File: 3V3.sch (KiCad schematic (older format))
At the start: 5 parts

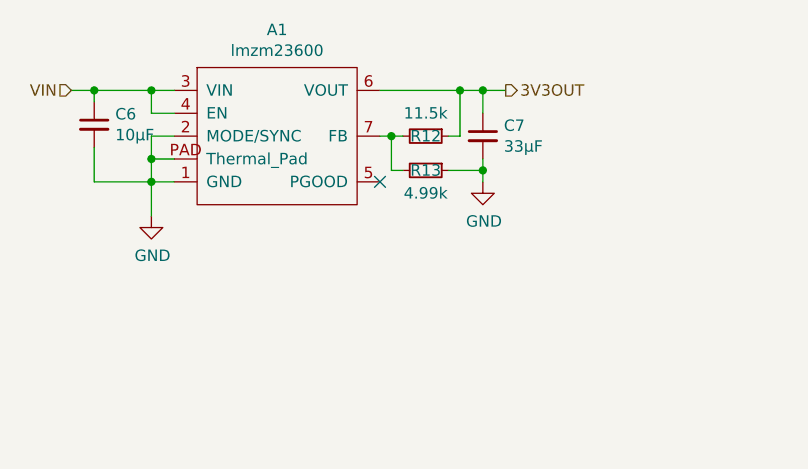
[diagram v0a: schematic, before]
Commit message: LMZM23600 from official kicad lib
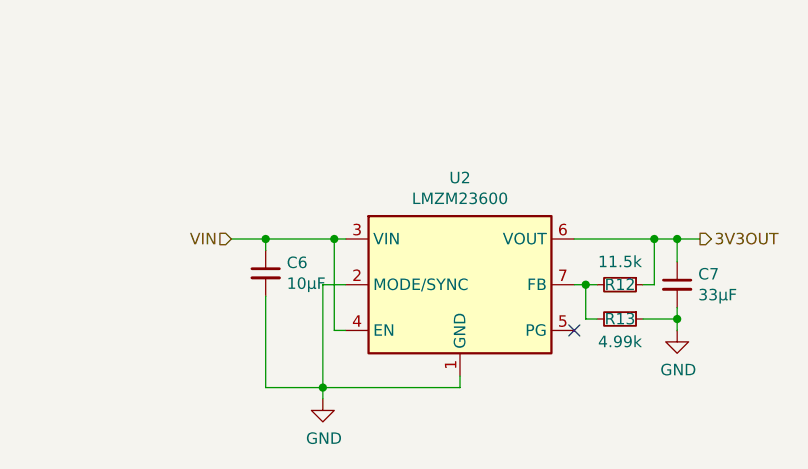
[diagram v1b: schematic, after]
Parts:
- removed A1: lmzm23600, LMZM23600:lmzm23600, symbol lmzm23600:lmzm23600
- added U2: LMZM23600, Package_LGA:Texas_SIL0010A_MicroSiP-10-1EP_3.8x3mm_P0.6mm_EP0.7x2.9mm_ThermalVias, symbol Regulator_Switching:LMZM23600
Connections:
- net 3V3OUT: now also U2.6 (VOUT)
- net GND: now also U2.1 (GND), U2.11 (GND), U2.2 (MODE/SYNC)
- net VIN: now also U2.3 (VIN), U2.4 (EN)
- net at R12.2, R13.2: now also U2.7 (FB)
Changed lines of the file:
@@
 $EndDescr
 $Comp
-L lmzm23600:lmzm23600 A?
-U 1 1 5C2CE8BB
-P 4350 2150
-AR Path="/5C2CE8BB" Ref="A?"  Part="1"
-AR Path="/5C2CDDAC/5C2CE8BB" Ref="A?"  Part="1"
-AR Path="/5C920C0A/5C2CE8BB" Ref="A1"  Part="1"
-F 0 "A1" H 4350 2615 50  0000 C CNN
-F 1 "lmzm23600" H 4350 2524 50  0000 C CNN
-F 2 "LMZM23600:lmzm23600" H 4350 2150 50  0001 C CNN
-F 3 "" H 4350 2150 50  0001 C CNN
-	1    4350 2150
-	1    0    0    -1
-$EndComp
-Wire Wire Line
-	3800 2250 3800 2350
-Wire Wire Line
-	3800 2350 3900 2350
-$Comp
-L power:GND #PWR?
-U 1 1 5C2CE8C4
-P 3800 2500
-AR Path="/5C2CE8C4" Ref="#PWR?"  Part="1"
-AR Path="/5C2CDDAC/5C2CE8C4" Ref="#PWR?"  Part="1"
-AR Path="/5C920C0A/5C2CE8C4" Ref="#PWR034"  Part="1"
-F 0 "#PWR034" H 3800 2250 50  0001 C CNN
-F 1 "GND" H 3805 2327 50  0000 C CNN
-F 2 "" H 3800 2500 50  0001 C CNN
-F 3 "" H 3800 2500 50  0001 C CNN
-	1    3800 2500
-	1    0    0    -1
-$EndComp
-Wire Wire Line
-	3800 2500 3800 2350
-Connection ~ 3800 2350
-$Comp
-L Device:C_Small C?
-U 1 1 5C2CE8DC
-P 3550 2100
-AR Path="/5C2CE8DC" Ref="C?"  Part="1"
-AR Path="/5C2CDDAC/5C2CE8DC" Ref="C?"  Part="1"
-AR Path="/5C920C0A/5C2CE8DC" Ref="C6"  Part="1"
-F 0 "C6" H 3642 2146 50  0000 L CNN
-F 1 "10µF" H 3642 2055 50  0000 L CNN
-F 2 "Capacitor_SMD:C_1210_3225Metric" H 3550 2100 50  0001 C CNN
-F 3 "~" H 3550 2100 50  0001 C CNN
-F 4 "50V" H 3550 2100 50  0001 C CNN "Voltage Rating"
-	1    3550 2100
-	1    0    0    -1
-$EndComp
-Wire Wire Line
-	3550 2200 3550 2350
-Wire Wire Line
-	3550 2350 3800 2350
-Wire Wire Line
-	3800 2150 3800 2250
-Connection ~ 3800 2250
-Wire Wire Line
-	3800 2150 3900 2150
-Wire Wire Line
-	3800 2250 3900 2250
-Wire Wire Line
-	3550 2000 3550 1950
-Wire Wire Line
-	3550 1950 3800 1950
-Connection ~ 3800 1950
-Wire Wire Line
-	3800 1950 3900 1950
-Wire Wire Line
-	3800 2050 3800 1950
-Wire Wire Line
-	3800 2050 3900 2050
-$Comp
-L Device:C_Small C?
-U 1 1 5C2CE8F0
-P 5250 2150
-AR Path="/5C2CE8F0" Ref="C?"  Part="1"
-AR Path="/5C2CDDAC/5C2CE8F0" Ref="C?"  Part="1"
-AR Path="/5C920C0A/5C2CE8F0" Ref="C7"  Part="1"
-F 0 "C7" H 5342 2196 50  0000 L CNN
-F 1 "33µF" H 5342 2105 50  0000 L CNN
-F 2 "Capacitor_SMD:C_1210_3225Metric" H 5250 2150 50  0001 C CNN
-F 3 "~" H 5250 2150 50  0001 C CNN
-F 4 "Low ESR" H 5250 2150 50  0001 C CNN "Notes"
-	1    5250 2150
+L Regulator_Switching:LMZM23600 U2
+U 1 1 5CA58FF1
+P 5150 2800
+F 0 "U2" H 5150 3267 50  0000 C CNN
+F 1 "LMZM23600" H 5150 3176 50  0000 C CNN
+F 2 "Package_LGA:Texas_SIL0010A_MicroSiP-10-1EP_3.8x3mm_P0.6mm_EP0.7x2.9mm_ThermalVias" H 5150 1950 50  0001 C CNN
+F 3 "http://www.ti.com/lit/ds/symlink/lmzm23600.pdf" H 5150 2050 50  0001 C CNN
+	1    5150 2800
 	1    0    0    -1
 $EndComp
 $Comp
 L power:GND #PWR?
-U 1 1 5C2CE8F8
-P 5250 2350
-AR Path="/5C2CE8F8" Ref="#PWR?"  Part="1"
-AR Path="/5C2CDDAC/5C2CE8F8" Ref="#PWR?"  Part="1"
-AR Path="/5C920C0A/5C2CE8F8" Ref="#PWR035"  Part="1"
-F 0 "#PWR035" H 5250 2100 50  0001 C CNN
-F 1 "GND" H 5255 2177 50  0000 C CNN
-F 2 "" H 5250 2350 50  0001 C CNN
-F 3 "" H 5250 2350 50  0001 C CNN
-	1    5250 2350
+U 1 1 5CA5C1D2
+P 4550 3300
+AR Path="/5CA5C1D2" Ref="#PWR?"  Part="1"
+AR Path="/5C2CDDAC/5CA5C1D2" Ref="#PWR?"  Part="1"
+AR Path="/5C920C0A/5CA5C1D2" Ref="#PWR034"  Part="1"
+F 0 "#PWR034" H 4550 3050 50  0001 C CNN
+F 1 "GND" H 4555 3127 50  0000 C CNN
+F 2 "" H 4550 3300 50  0001 C CNN
+F 3 "" H 4550 3300 50  0001 C CNN
+	1    4550 3300
+	1    0    0    -1
+$EndComp
+$Comp
+L Device:C_Small C?
+U 1 1 5CA5C1DF
+P 4300 2750
+AR Path="/5CA5C1DF" Ref="C?"  Part="1"
+AR Path="/5C2CDDAC/5CA5C1DF" Ref="C?"  Part="1"
+AR Path="/5C920C0A/5CA5C1DF" Ref="C6"  Part="1"
+F 0 "C6" H 4392 2796 50  0000 L CNN
+F 1 "10µF" H 4392 2705 50  0000 L CNN
+F 2 "Capacitor_SMD:C_1210_3225Metric" H 4300 2750 50  0001 C CNN
+F 3 "~" H 4300 2750 50  0001 C CNN
+F 4 "50V" H 4300 2750 50  0001 C CNN "Voltage Rating"
+	1    4300 2750
+	1    0    0    -1
+$EndComp
+$Comp
+L Device:C_Small C?
+U 1 1 5CA5C1F6
+P 6100 2800
+AR Path="/5CA5C1F6" Ref="C?"  Part="1"
+AR Path="/5C2CDDAC/5CA5C1F6" Ref="C?"  Part="1"
+AR Path="/5C920C0A/5CA5C1F6" Ref="C7"  Part="1"
+F 0 "C7" H 6192 2846 50  0000 L CNN
+F 1 "33µF" H 6192 2755 50  0000 L CNN
+F 2 "Capacitor_SMD:C_1210_3225Metric" H 6100 2800 50  0001 C CNN
+F 3 "~" H 6100 2800 50  0001 C CNN
+F 4 "Low ESR" H 6100 2800 50  0001 C CNN "Notes"
+	1    6100 2800
+	1    0    0    -1
+$EndComp
+$Comp
+L power:GND #PWR?
+U 1 1 5CA5C200
+P 6100 3000
+AR Path="/5CA5C200" Ref="#PWR?"  Part="1"
+AR Path="/5C2CDDAC/5CA5C200" Ref="#PWR?"  Part="1"
+AR Path="/5C920C0A/5CA5C200" Ref="#PWR035"  Part="1"
+F 0 "#PWR035" H 6100 2750 50  0001 C CNN
+F 1 "GND" H 6105 2827 50  0000 C CNN
+F 2 "" H 6100 3000 50  0001 C CNN
+F 3 "" H 6100 3000 50  0001 C CNN
+	1    6100 3000
 	1    0    0    -1
 $EndComp
 Wire Wire Line
-	5250 2050 5250 1950
+	6100 2700 6100 2600
 Wire Wire Line
-	5250 2250 5250 2300
+	6100 2900 6100 2950
 $Comp
 L Device:R_Small R?
-U 1 1 5C2CE900
-P 5000 2150
-AR Path="/5C2CE900" Ref="R?"  Part="1"
-AR Path="/5C2CDDAC/5C2CE900" Ref="R?"  Part="1"
-AR Path="/5C920C0A/5C2CE900" Ref="R12"  Part="1"
-F 0 "R12" V 5000 2150 50  0000 C CNN
-F 1 "11.5k" V 4900 2150 50  0000 C CNN
-F 2 "Resistor_SMD:R_0603_1608Metric" H 5000 2150 50  0001 C CNN
-F 3 "~" H 5000 2150 50  0001 C CNN
-	1    5000 2150
+U 1 1 5CA5C20C
+P 5850 2800
+AR Path="/5CA5C20C" Ref="R?"  Part="1"
+AR Path="/5C2CDDAC/5CA5C20C" Ref="R?"  Part="1"
+AR Path="/5C920C0A/5CA5C20C" Ref="R12"  Part="1"
+F 0 "R12" V 5850 2800 50  0000 C CNN
+F 1 "11.5k" V 5750 2800 50  0000 C CNN
+F 2 "Resistor_SMD:R_0603_1608Metric" H 5850 2800 50  0001 C CNN
+F 3 "~" H 5850 2800 50  0001 C CNN
+	1    5850 2800
 	0    1    1    0
 $EndComp
 Wire Wire Line
-	4800 2150 4850 2150
+	5650 2800 5700 2800
 $Comp
 L Device:R_Small R?
-U 1 1 5C2CE909
-P 5000 2300
-AR Path="/5C2CE909" Ref="R?"  Part="1"
-AR Path="/5C2CDDAC/5C2CE909" Ref="R?"  Part="1"
-AR Path="/5C920C0A/5C2CE909" Ref="R13"  Part="1"
-F 0 "R13" V 5000 2300 50  0000 C CNN
-F 1 "4.99k" V 5100 2300 50  0000 C CNN
-F 2 "Resistor_SMD:R_0603_1608Metric" H 5000 2300 50  0001 C CNN
-F 3 "~" H 5000 2300 50  0001 C CNN
-	1    5000 2300
+U 1 1 5CA5C217
+P 5850 2950
+AR Path="/5CA5C217" Ref="R?"  Part="1"
+AR Path="/5C2CDDAC/5CA5C217" Ref="R?"  Part="1"
+AR Path="/5C920C0A/5CA5C217" Ref="R13"  Part="1"
+F 0 "R13" V 5850 2950 50  0000 C CNN
+F 1 "4.99k" V 5950 2950 50  0000 C CNN
+F 2 "Resistor_SMD:R_0603_1608Metric" H 5850 2950 50  0001 C CNN
+F 3 "~" H 5850 2950 50  0001 C CNN
+	1    5850 2950
 	0    1    1    0
 $EndComp
 Wire Wire Line
-	4900 2300 4850 2300
+	5750 2950 5700 2950
 Wire Wire Line
-	4850 2300 4850 2150
-Connection ~ 4850 2150
+	5700 2950 5700 2800
+Connection ~ 5700 2800
 Wire Wire Line
-	4850 2150 4900 2150
+	5700 2800 5750 2800
 Wire Wire Line
-	5100 2300 5250 2300
-Connection ~ 5250 2300
+	5950 2950 6100 2950
+Connection ~ 6100 2950
 Wire Wire Line
-	5250 2300 5250 2350
+	6100 2950 6100 3000
 Wire Wire Line
-	5100 2150 5150 2150
+	5950 2800 6000 2800
 Wire Wire Line
-	5150 2150 5150 1950
-Connection ~ 5150 1950
+	6000 2800 6000 2600
+Connection ~ 6000 2600
 Wire Wire Line
-	5150 1950 5250 1950
-NoConn ~ 4800 2350
-Text HLabel 3450 1950 0    50   Input ~ 0
+	6000 2600 6100 2600
+NoConn ~ 5650 3000
+Text HLabel 4150 2600 0    50   Input ~ 0
 VIN
-Wire Wire Line
-	3450 1950 3550 1950
-Connection ~ 3550 1950
-Text HLabel 5350 1950 2    50   Output ~ 0
+Text HLabel 6200 2600 2    50   Output ~ 0
 3V3OUT
 Wire Wire Line
-	4800 1950 5150 1950
+	5650 2600 6000 2600
 Wire Wire Line
-	5250 1950 5350 1950
-Connection ~ 5250 1950
+	6100 2600 6200 2600
+Connection ~ 6100 2600
+Wire Wire Line
+	4650 2600 4600 2600
+Wire Wire Line
+	4300 2650 4300 2600
+Connection ~ 4300 2600
+Wire Wire Line
+	4300 2600 4150 2600
+Wire Wire Line
+	4650 3000 4600 3000
+Wire Wire Line
+	4600 3000 4600 2600
+Connection ~ 4600 2600
+Wire Wire Line
+	4600 2600 4300 2600
+Wire Wire Line
+	4650 2800 4550 2800
+Wire Wire Line
+	4550 2800 4550 3250
+Wire Wire Line
+	4550 3250 5150 3250
+Wire Wire Line
+	5150 3250 5150 3200
+Wire Wire Line
+	4300 3250 4550 3250
+Wire Wire Line
+	4300 2850 4300 3250
+Connection ~ 4550 3250
+Wire Wire Line
+	4550 3300 4550 3250
 $EndSCHEMATC

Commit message: use submodule for FT230
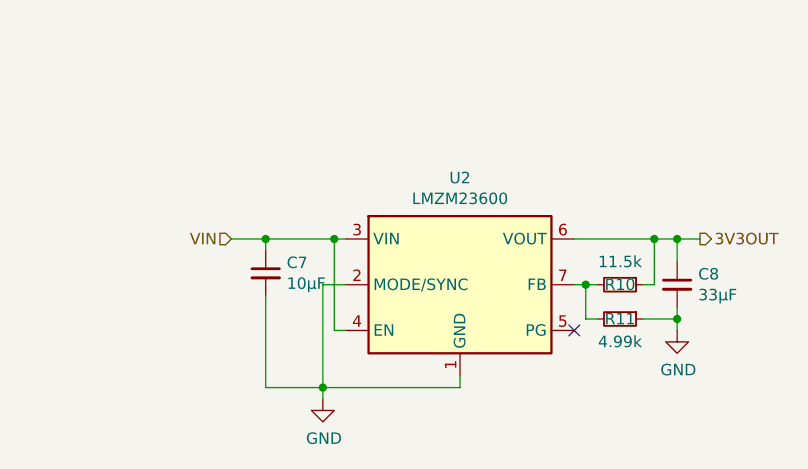
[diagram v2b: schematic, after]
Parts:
- renumbered C6 to C7, C7 to C8, R12 to R10, R13 to R11
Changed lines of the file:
@@
 AR Path="/5CA5C1DF" Ref="C?"  Part="1"
 AR Path="/5C2CDDAC/5CA5C1DF" Ref="C?"  Part="1"
-AR Path="/5C920C0A/5CA5C1DF" Ref="C6"  Part="1"
-F 0 "C6" H 4392 2796 50  0000 L CNN
+AR Path="/5C920C0A/5CA5C1DF" Ref="C7"  Part="1"
+F 0 "C7" H 4392 2796 50  0000 L CNN
 F 1 "10µF" H 4392 2705 50  0000 L CNN
 F 2 "Capacitor_SMD:C_1210_3225Metric" H 4300 2750 50  0001 C CNN
@@
 AR Path="/5CA5C1F6" Ref="C?"  Part="1"
 AR Path="/5C2CDDAC/5CA5C1F6" Ref="C?"  Part="1"
-AR Path="/5C920C0A/5CA5C1F6" Ref="C7"  Part="1"
-F 0 "C7" H 6192 2846 50  0000 L CNN
+AR Path="/5C920C0A/5CA5C1F6" Ref="C8"  Part="1"
+F 0 "C8" H 6192 2846 50  0000 L CNN
 F 1 "33µF" H 6192 2755 50  0000 L CNN
 F 2 "Capacitor_SMD:C_1210_3225Metric" H 6100 2800 50  0001 C CNN
@@
 AR Path="/5CA5C20C" Ref="R?"  Part="1"
 AR Path="/5C2CDDAC/5CA5C20C" Ref="R?"  Part="1"
-AR Path="/5C920C0A/5CA5C20C" Ref="R12"  Part="1"
-F 0 "R12" V 5850 2800 50  0000 C CNN
+AR Path="/5C920C0A/5CA5C20C" Ref="R10"  Part="1"
+F 0 "R10" V 5850 2800 50  0000 C CNN
 F 1 "11.5k" V 5750 2800 50  0000 C CNN
 F 2 "Resistor_SMD:R_0603_1608Metric" H 5850 2800 50  0001 C CNN
@@
 AR Path="/5CA5C217" Ref="R?"  Part="1"
 AR Path="/5C2CDDAC/5CA5C217" Ref="R?"  Part="1"
-AR Path="/5C920C0A/5CA5C217" Ref="R13"  Part="1"
-F 0 "R13" V 5850 2950 50  0000 C CNN
+AR Path="/5C920C0A/5CA5C217" Ref="R11"  Part="1"
+F 0 "R11" V 5850 2950 50  0000 C CNN
 F 1 "4.99k" V 5950 2950 50  0000 C CNN
 F 2 "Resistor_SMD:R_0603_1608Metric" H 5850 2950 50  0001 C CNN

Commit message: pullups, jumpers
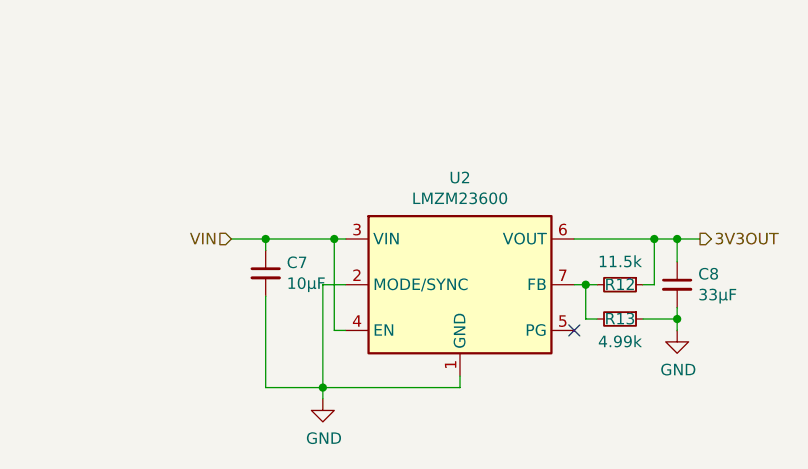
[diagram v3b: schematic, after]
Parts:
- renumbered R10 to R12, R11 to R13
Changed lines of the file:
@@
 AR Path="/5CA5C20C" Ref="R?"  Part="1"
 AR Path="/5C2CDDAC/5CA5C20C" Ref="R?"  Part="1"
-AR Path="/5C920C0A/5CA5C20C" Ref="R10"  Part="1"
-F 0 "R10" V 5850 2800 50  0000 C CNN
+AR Path="/5C920C0A/5CA5C20C" Ref="R12"  Part="1"
+F 0 "R12" V 5850 2800 50  0000 C CNN
 F 1 "11.5k" V 5750 2800 50  0000 C CNN
 F 2 "Resistor_SMD:R_0603_1608Metric" H 5850 2800 50  0001 C CNN
@@
 AR Path="/5CA5C217" Ref="R?"  Part="1"
 AR Path="/5C2CDDAC/5CA5C217" Ref="R?"  Part="1"
-AR Path="/5C920C0A/5CA5C217" Ref="R11"  Part="1"
-F 0 "R11" V 5850 2950 50  0000 C CNN
+AR Path="/5C920C0A/5CA5C217" Ref="R13"  Part="1"
+F 0 "R13" V 5850 2950 50  0000 C CNN
 F 1 "4.99k" V 5950 2950 50  0000 C CNN
 F 2 "Resistor_SMD:R_0603_1608Metric" H 5850 2950 50  0001 C CNN

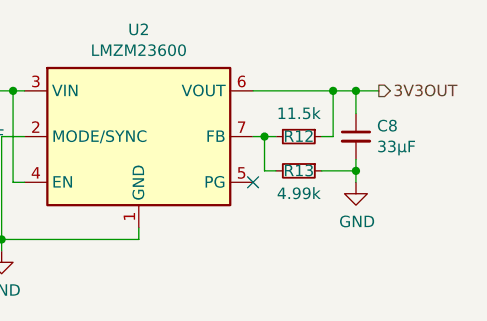
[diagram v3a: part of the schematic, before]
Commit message: small layout fixes
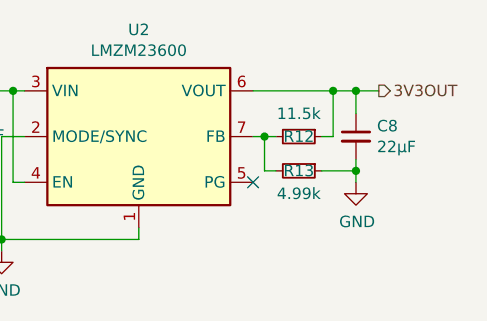
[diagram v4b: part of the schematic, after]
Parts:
- C8: value 33µF -> 22µF; footprint Capacitor_SMD:C_1210_3225Metric -> Capacitor_SMD:C_1206_3216Metric
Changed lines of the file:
@@
 AR Path="/5C920C0A/5CA5C1F6" Ref="C8"  Part="1"
 F 0 "C8" H 6192 2846 50  0000 L CNN
-F 1 "33µF" H 6192 2755 50  0000 L CNN
-F 2 "Capacitor_SMD:C_1210_3225Metric" H 6100 2800 50  0001 C CNN
+F 1 "22µF" H 6192 2755 50  0000 L CNN
+F 2 "Capacitor_SMD:C_1206_3216Metric" H 6100 2800 50  0001 C CNN
 F 3 "~" H 6100 2800 50  0001 C CNN
 F 4 "Low ESR" H 6100 2800 50  0001 C CNN "Notes"
